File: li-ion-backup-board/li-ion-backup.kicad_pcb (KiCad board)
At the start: 2 copper layers, 100.1 x 89.9 mm, 75 parts, among them J1 18650_IN, J2 Input_01x02, J3 24V, Q1 Si2302DS, Q2 Si2302DS, Q3 Si2302DS, U1 MT3608, U2 LM2596S-ADJ, U3 DW01A, U4 TP4056

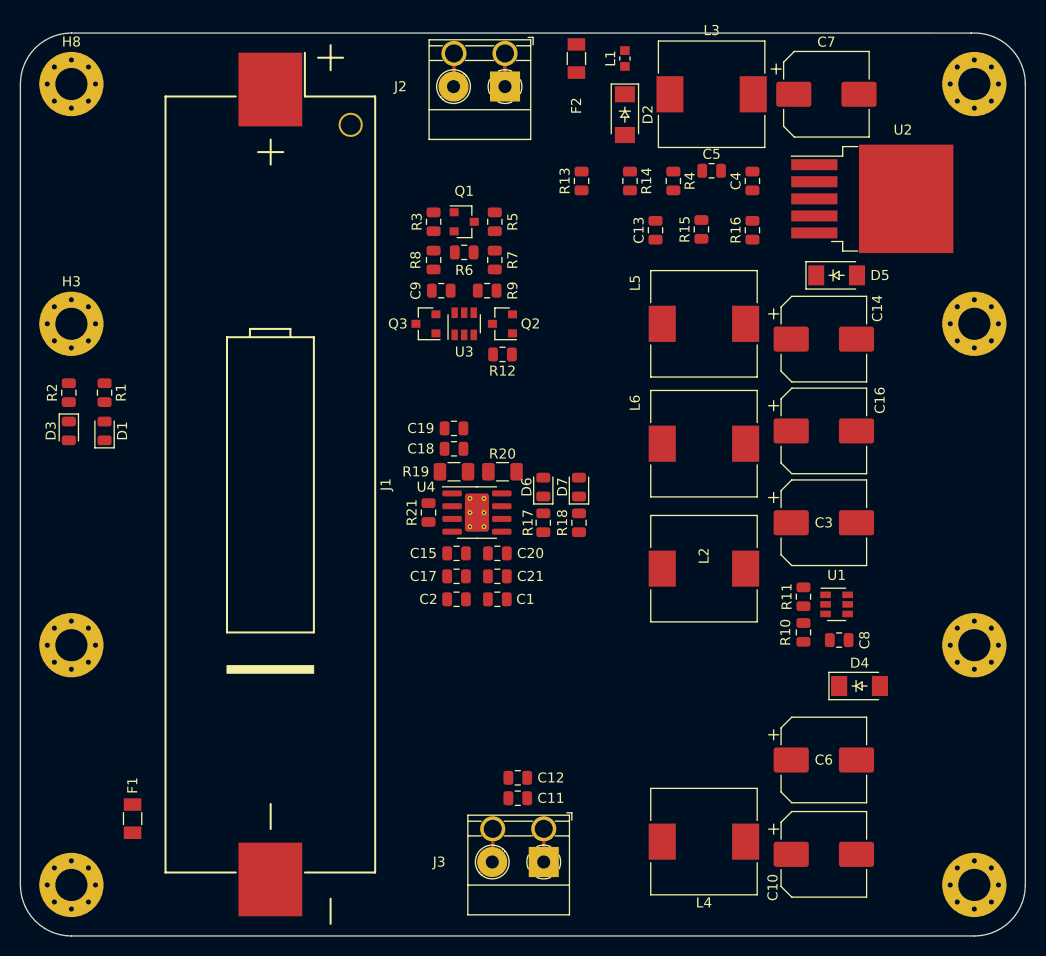
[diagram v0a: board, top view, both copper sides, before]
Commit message: add gerbers and production files
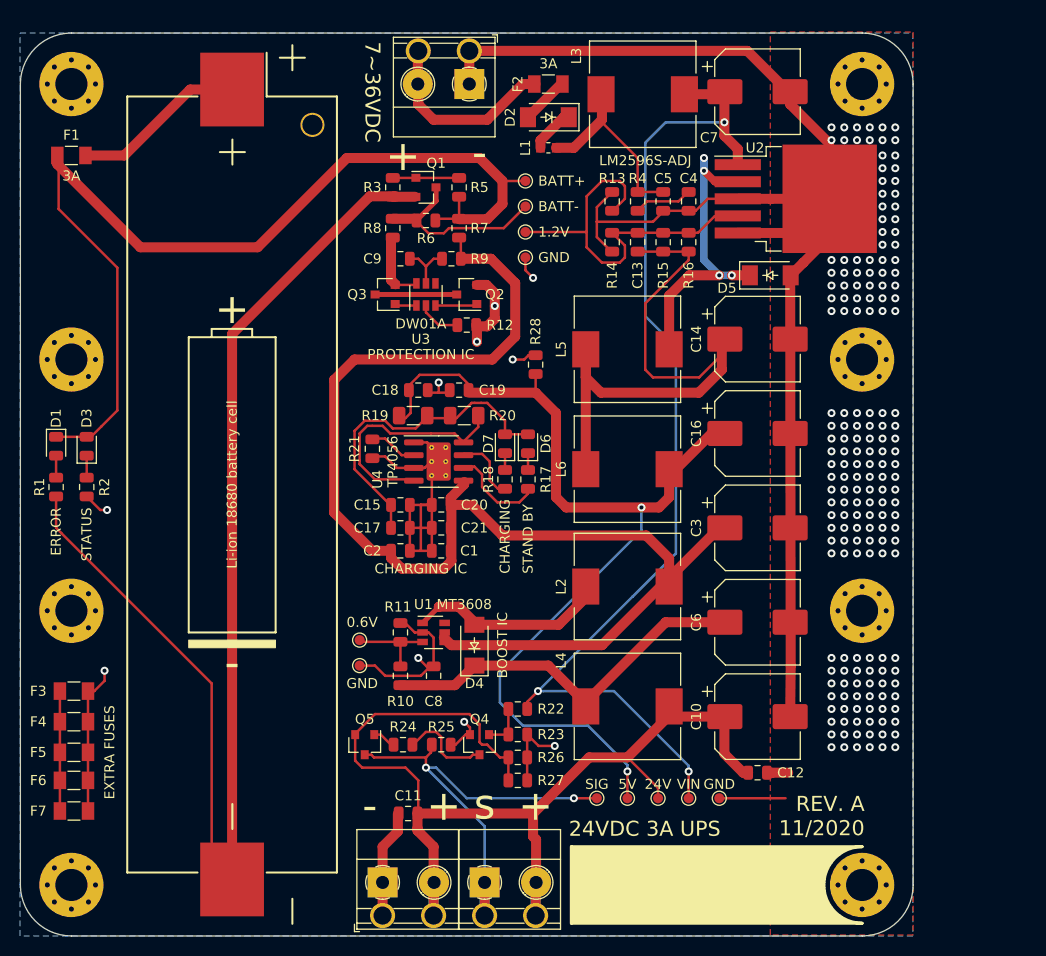
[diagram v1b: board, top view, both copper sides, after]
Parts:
- added F3: Fuse, e-Power:FUSE_1206_3216Metric, F.Cu at (157.7, 124.5)
- added F4: Fuse, e-Power:FUSE_1206_3216Metric, F.Cu at (157.7, 127.5)
- added F5: Fuse, e-Power:FUSE_1206_3216Metric, F.Cu at (157.7, 130.6)
- added F6: Fuse, e-Power:FUSE_1206_3216Metric, F.Cu at (157.7, 133.3)
- added F7: Fuse, e-Power:FUSE_1206_3216Metric, F.Cu at (157.7, 136.4)
- added J4: OUT_SIG, e-Power:TerminalBlock_Phoenix_MKDS-1,5-2_1x02_P5.08mm_Horizontal_3D, F.Cu at (198.6, 143.5)
- added Q4: MMBT5551, Package_TO_SOT_SMD:SOT-23, F.Cu at (198.1, 129.8)
- added Q5: MMBT5401, Package_TO_SOT_SMD:SOT-23, F.Cu at (186.7, 129.8)
- added R22: 10K, Resistor_SMD:R_0805_2012Metric, F.Cu at (201.9, 126.2)
- added R23: 1K, Resistor_SMD:R_0805_2012Metric, F.Cu at (201.9, 128.8)
- added R24: 10K, Resistor_SMD:R_0805_2012Metric, F.Cu at (190.5, 129.8)
- added R25: 10K, Resistor_SMD:R_0805_2012Metric, F.Cu at (194.3, 129.8)
- added R26: 10K, Resistor_SMD:R_0805_2012Metric, F.Cu at (201.9, 131.1)
- added R27: 10K, Resistor_SMD:R_0805_2012Metric, F.Cu at (201.9, 133.3)
- added R28: 1K, Resistor_SMD:R_0805_2012Metric, F.Cu at (203.7, 91.9)
- added TP1: BATT+, e-Power:TestPoint_Pad_D1.0mm, F.Cu at (202.7, 73.7)
- added TP10: GND, e-Power:TestPoint_Pad_D1.0mm, F.Cu at (202.7, 81.3)
- added TP11: GND, e-Power:TestPoint_Pad_D1.0mm, F.Cu at (186.2, 121.9)
- added TP2: BATT-, e-Power:TestPoint_Pad_D1.0mm, F.Cu at (202.7, 76.2)
- added TP3: VIN, e-Power:TestPoint_Pad_D1.0mm, F.Cu at (218.9, 135.1)
- added TP4: 0.6V, e-Power:TestPoint_Pad_D1.0mm, F.Cu at (186.2, 119.4)
- added TP5: 1.2V, e-Power:TestPoint_Pad_D1.0mm, F.Cu at (202.7, 78.7)
- added TP6: 24V, e-Power:TestPoint_Pad_D1.0mm, F.Cu at (215.9, 135.1)
- added TP7: SIG, e-Power:TestPoint_Pad_D1.0mm, F.Cu at (209.8, 135.1)
- added TP8: 5V, e-Power:TestPoint_Pad_D1.0mm, F.Cu at (212.9, 135.1)
- added TP9: GND, e-Power:TestPoint_Pad_D1.0mm, F.Cu at (222.0, 135.1)
- L2, L3, L4, L5, L6: value 15uH -> 10uH
- moved F1 66.3 mm to (157.5, 71.1), turned to 0 degrees
- moved C8 40.5 mm to (193.5, 122.9), turned to 90 degrees
- moved R10 40.4 mm to (190.2, 122.9)
- moved R11 40.3 mm to (190.2, 118.6)
- moved U1 40.2 mm to (193.5, 118.6)
- moved D4 38.6 mm to (197.6, 119.9), turned to 90 degrees
- moved C12 23.9 mm to (225.8, 132.6), turned to 0 degrees
- moved J3 16.2 mm to (188.5, 143.5), turned to 0 degrees
- moved L4 15.5 mm to (212.9, 126.0)
- moved C10 15.2 mm to (225.8, 127.0)
- moved C6 15.2 mm to (225.8, 117.6)
- moved H1 11.7 mm to (236.2, 91.4)
- moved L1 11.7 mm to (205.0, 70.4), turned to 0 degrees
- moved H2 11.7 mm to (236.2, 116.5)
- moved H5 11.2 mm to (236.2, 143.8)
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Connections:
- net Net-(C7-Pad1) renamed /VIN
- J1 pad 1: Net-(J1-Pad1) -> Net-(F1-Pad2)
- J1 pad 2: Net-(F1-Pad2) -> Net-(J1-Pad2)
- J3 pad 1: +24V -> GND
- J3 pad 2: GND -> +24V
- Q1 pad 2: Net-(J1-Pad1) -> Net-(J1-Pad2)
- R1 pad 1: Net-(J1-Pad1) -> Net-(J1-Pad2)
- R2 pad 2: Net-(J1-Pad1) -> GND
- R3 pad 1: Net-(J1-Pad1) -> Net-(J1-Pad2)
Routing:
- net GND: track 0.00 -> 257.5 mm, vias 0 -> 188
- net /BATT+: track 0.00 -> 135.1 mm
- net Net-(J1-Pad2): track 0.00 -> 123.6 mm
- net +24V: track 0.00 -> 110.2 mm
- net /VIN: track 0.00 -> 105.4 mm, vias 0 -> 3
- net Net-(D1-Pad1): track 0.00 -> 102.5 mm
- net +5V: track 0.00 -> 97.3 mm, vias 0 -> 2
- net Net-(C13-Pad1): track 0.00 -> 62.6 mm
- net Net-(J4-Pad1): track 0.00 -> 47.4 mm, vias 0 -> 2
- net Net-(C13-Pad2): track 0.00 -> 39.9 mm
- net Net-(C6-Pad1): track 0.00 -> 38.3 mm
- net Net-(C15-Pad2): track 0.00 -> 32.7 mm
- net Net-(D5-Pad1): track 0.00 -> 31.6 mm, vias 0 -> 4
- net Net-(R20-Pad1): track 0.00 -> 23.8 mm
- net Net-(D4-Pad2): track 0.00 -> 19.8 mm
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- added copper zone on B.Cu, net GND
- added copper zone on F.Cu, net GND
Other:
- board size 100.1 x 89.9 mm -> 88.9 x 89.9 mm
- board text added: "+"
- board text added: "-"
- board text added: "24VDC 3A UPS"
- board text added: "7~~36VDC"
- board text added: "BOOST IC"
- board text added: "CHARGING"
- board text added: "CHARGING IC"
- board text added: "ERROR"
- board text added: "EXTRA FUSES"
- board text added: "PROTECTION IC"
- board text added: "REV. A 11/2020"
- board text added: "STAND BY"
- board text added: "STATUS"
- board text added: "s"
